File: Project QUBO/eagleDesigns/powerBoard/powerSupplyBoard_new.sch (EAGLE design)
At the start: 146 parts

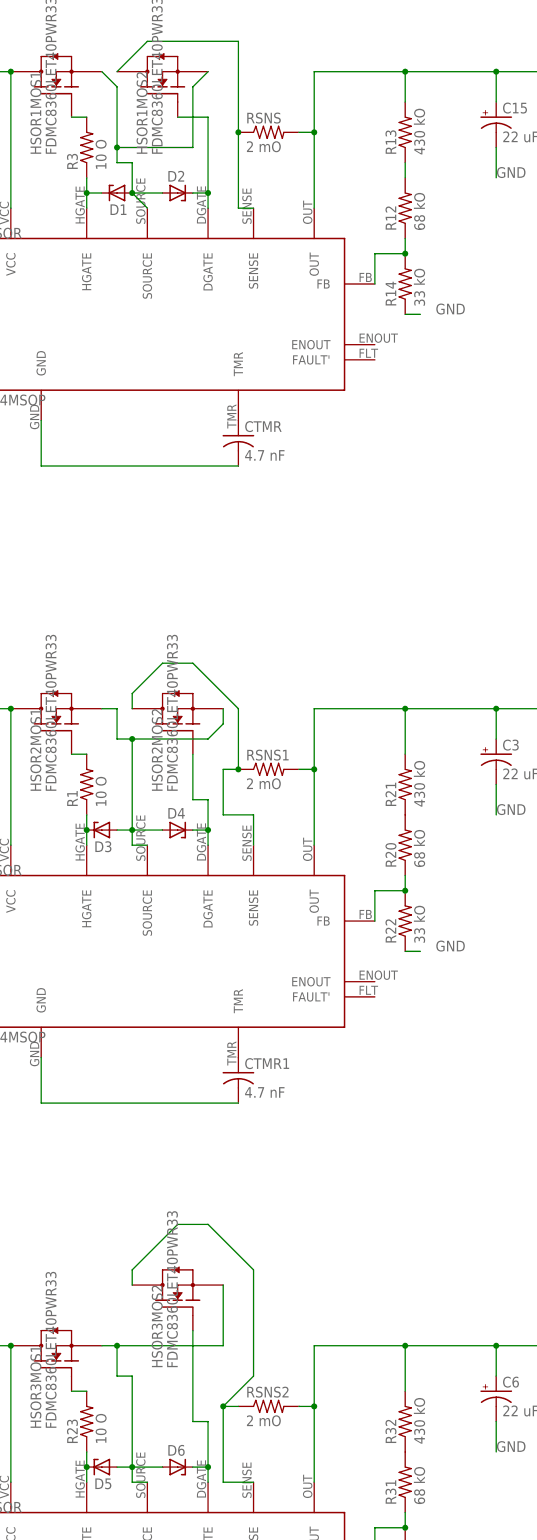
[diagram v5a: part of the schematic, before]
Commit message: got rid of sense resistor on psb
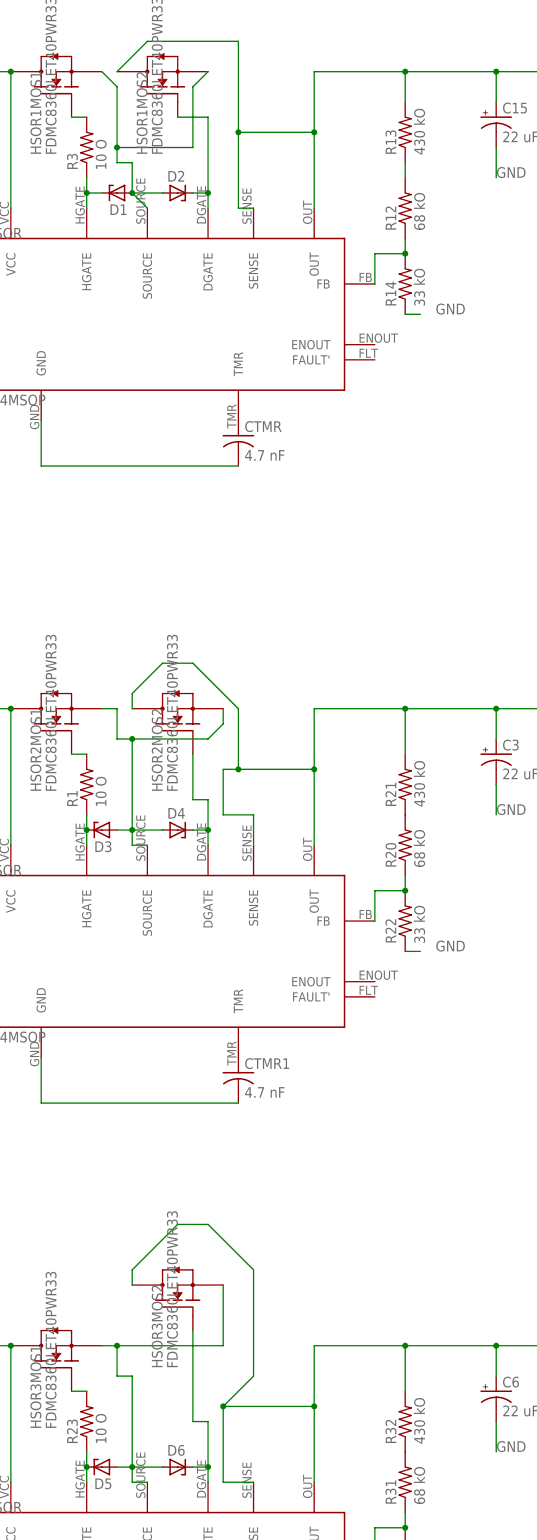
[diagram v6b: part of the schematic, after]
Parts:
- removed RSNS, RSNS1, RSNS2: 2 mO, resistor:R-US_R0805
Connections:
- removed net N$1: BAT1HSOR.SENSE, HSOR1MOS2.DRAIN, RSNS.1
- removed net N$43: BAT3HSOR.SENSE, HSOR3MOS2.DRAIN, RSNS2.1
- removed net N$5: BAT2HSOR.SENSE, HSOR2MOS2.DRAIN, RSNS1.1
- net BAT1HSOROUT: now also BAT1HSOR.SENSE, HSOR1MOS2.DRAIN; no longer RSNS.2
- net BAT2HSOROUT: now also BAT2HSOR.SENSE, HSOR2MOS2.DRAIN; no longer RSNS1.2
- net BAT3HSOROUT: now also BAT3HSOR.SENSE, HSOR3MOS2.DRAIN; no longer RSNS2.2
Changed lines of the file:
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@@
 <part name="R13" library="resistor" deviceset="R-US_" device="R0805" value="430 kO"/>
 <part name="R14" library="resistor" deviceset="R-US_" device="R0805" value="33 kO"/>
-<part name="RSNS" library="resistor" deviceset="R-US_" device="R0805" value="2 mO"/>
 <part name="CTMR" library="resistor" deviceset="C-US" device="C0805" value="4.7 nF"/>
 <part name="C15" library="resistor" deviceset="CPOL-US" device="F" value="22 uF"/>
@@
 <part name="R21" library="resistor" deviceset="R-US_" device="R0805" value="430 kO"/>
 <part name="R22" library="resistor" deviceset="R-US_" device="R0805" value="33 kO"/>
-<part name="RSNS1" library="resistor" deviceset="R-US_" device="R0805" value="2 mO"/>
 <part name="CTMR1" library="resistor" deviceset="C-US" device="C0805" value="4.7 nF"/>
 <part name="C3" library="resistor" deviceset="CPOL-US" device="F" value="22 uF"/>
@@
 <part name="R32" library="resistor" deviceset="R-US_" device="R0805" value="430 kO"/>
 <part name="R33" library="resistor" deviceset="R-US_" device="R0805" value="33 kO"/>
-<part name="RSNS2" library="resistor" deviceset="R-US_" device="R0805" value="2 mO"/>
 <part name="CTMR2" library="resistor" deviceset="C-US" device="C0805" value="4.7 nF"/>
 <part name="C6" library="resistor" deviceset="CPOL-US" device="F" value="22 uF"/>
@@
 <instance part="R13" gate="G$1" x="-116.84" y="121.92" rot="R90"/>
 <instance part="R14" gate="G$1" x="-116.84" y="96.52" rot="R90"/>
-<instance part="RSNS" gate="G$1" x="-139.7" y="121.92"/>
 <instance part="CTMR" gate="G$1" x="-144.78" y="71.12"/>
 <instance part="C15" gate="G$1" x="-101.6" y="124.46"/>
@@
 <instance part="R21" gate="G$1" x="-116.84" y="12.7" rot="R90"/>
 <instance part="R22" gate="G$1" x="-116.84" y="-10.16" rot="R90"/>
-<instance part="RSNS1" gate="G$1" x="-139.7" y="15.24"/>
 <instance part="CTMR1" gate="G$1" x="-144.78" y="-35.56"/>
 <instance part="C3" gate="G$1" x="-101.6" y="17.78"/>
@@
 <instance part="R32" gate="G$1" x="-116.84" y="-93.98" rot="R90"/>
 <instance part="R33" gate="G$1" x="-116.84" y="-116.84" rot="R90"/>
-<instance part="RSNS2" gate="G$1" x="-139.7" y="-91.44"/>
 <instance part="CTMR2" gate="G$1" x="-144.78" y="-142.24"/>
 <instance part="C6" gate="G$1" x="-101.6" y="-88.9"/>
@@
 <net name="BAT1HSOROUT" class="0">
 <segment>
-<pinref part="RSNS" gate="G$1" pin="2"/>
 <pinref part="BAT1HSOR" gate="G$1" pin="OUT"/>
-<wire x1="-134.62" y1="121.92" x2="-132.08" y2="121.92" width="0.1524" layer="91"/>
 <wire x1="-132.08" y1="121.92" x2="-132.08" y2="109.22" width="0.1524" layer="91"/>
 <wire x1="-132.08" y1="121.92" x2="-132.08" y2="132.08" width="0.1524" layer="91"/>
@@
 <junction x="-101.6" y="132.08"/>
 <pinref part="BAT1CS" gate="G$1" pin="IP+"/>
+<pinref part="BAT1HSOR" gate="G$1" pin="SENSE"/>
+<wire x1="-142.24" y1="109.22" x2="-144.78" y2="109.22" width="0.1524" layer="91"/>
+<wire x1="-144.78" y1="137.16" x2="-144.78" y2="121.92" width="0.1524" layer="91"/>
+<pinref part="HSOR1MOS2" gate="G$1" pin="DRAIN"/>
+<wire x1="-144.78" y1="121.92" x2="-144.78" y2="109.22" width="0.1524" layer="91"/>
+<wire x1="-165.1" y1="132.08" x2="-160.02" y2="137.16" width="0.1524" layer="91"/>
+<wire x1="-160.02" y1="137.16" x2="-144.78" y2="137.16" width="0.1524" layer="91"/>
+<wire x1="-132.08" y1="121.92" x2="-144.78" y2="121.92" width="0.1524" layer="91"/>
+<junction x="-144.78" y="121.92"/>
 </segment>
 </net>
@@
 </segment>
 </net>
-<net name="N$5" class="0">
-<segment>
-<pinref part="BAT2HSOR" gate="G$1" pin="SENSE"/>
-<wire x1="-142.24" y1="7.62" x2="-142.24" y2="2.54" width="0.1524" layer="91"/>
-<wire x1="-142.24" y1="7.62" x2="-147.32" y2="7.62" width="0.1524" layer="91"/>
-<wire x1="-147.32" y1="7.62" x2="-147.32" y2="15.24" width="0.1524" layer="91"/>
-<pinref part="RSNS1" gate="G$1" pin="1"/>
-<wire x1="-144.78" y1="15.24" x2="-147.32" y2="15.24" width="0.1524" layer="91"/>
-<pinref part="HSOR2MOS2" gate="G$1" pin="DRAIN"/>
-<wire x1="-162.56" y1="25.4" x2="-162.56" y2="27.94" width="0.1524" layer="91"/>
-<wire x1="-162.56" y1="27.94" x2="-157.48" y2="33.02" width="0.1524" layer="91"/>
-<wire x1="-157.48" y1="33.02" x2="-152.4" y2="33.02" width="0.1524" layer="91"/>
-<wire x1="-152.4" y1="33.02" x2="-144.78" y2="25.4" width="0.1524" layer="91"/>
-<wire x1="-144.78" y1="25.4" x2="-144.78" y2="15.24" width="0.1524" layer="91"/>
-<junction x="-144.78" y="15.24"/>
-</segment>
-</net>
 <net name="N$6" class="0">
 <segment>
@@
 <net name="BAT2HSOROUT" class="0">
 <segment>
-<pinref part="RSNS1" gate="G$1" pin="2"/>
 <pinref part="BAT2HSOR" gate="G$1" pin="OUT"/>
-<wire x1="-134.62" y1="15.24" x2="-132.08" y2="15.24" width="0.1524" layer="91"/>
 <wire x1="-132.08" y1="15.24" x2="-132.08" y2="2.54" width="0.1524" layer="91"/>
 <wire x1="-132.08" y1="15.24" x2="-132.08" y2="25.4" width="0.1524" layer="91"/>
@@
 <junction x="-101.6" y="25.4"/>
 <pinref part="BAT2CS" gate="G$1" pin="IP+"/>
+<pinref part="BAT2HSOR" gate="G$1" pin="SENSE"/>
+<wire x1="-142.24" y1="7.62" x2="-142.24" y2="2.54" width="0.1524" layer="91"/>
+<wire x1="-142.24" y1="7.62" x2="-147.32" y2="7.62" width="0.1524" layer="91"/>
+<wire x1="-147.32" y1="7.62" x2="-147.32" y2="15.24" width="0.1524" layer="91"/>
+<wire x1="-144.78" y1="15.24" x2="-147.32" y2="15.24" width="0.1524" layer="91"/>
+<pinref part="HSOR2MOS2" gate="G$1" pin="DRAIN"/>
+<wire x1="-162.56" y1="25.4" x2="-162.56" y2="27.94" width="0.1524" layer="91"/>
+<wire x1="-162.56" y1="27.94" x2="-157.48" y2="33.02" width="0.1524" layer="91"/>
+<wire x1="-157.48" y1="33.02" x2="-152.4" y2="33.02" width="0.1524" layer="91"/>
+<wire x1="-152.4" y1="33.02" x2="-144.78" y2="25.4" width="0.1524" layer="91"/>
+<wire x1="-144.78" y1="25.4" x2="-144.78" y2="15.24" width="0.1524" layer="91"/>
+<wire x1="-132.08" y1="15.24" x2="-144.78" y2="15.24" width="0.1524" layer="91"/>
+<junction x="-144.78" y="15.24"/>
 </segment>
 </net>
@@
 <net name="BAT3HSOROUT" class="0">
 <segment>
-<pinref part="RSNS2" gate="G$1" pin="2"/>
 <pinref part="BAT3HSOR" gate="G$1" pin="OUT"/>
-<wire x1="-134.62" y1="-91.44" x2="-132.08" y2="-91.44" width="0.1524" layer="91"/>
 <wire x1="-132.08" y1="-91.44" x2="-132.08" y2="-104.14" width="0.1524" layer="91"/>
 <wire x1="-132.08" y1="-91.44" x2="-132.08" y2="-81.28" width="0.1524" layer="91"/>
@@
 <junction x="-101.6" y="-81.28"/>
 <pinref part="BAT3CS" gate="G$1" pin="IP+"/>
+<pinref part="BAT3HSOR" gate="G$1" pin="SENSE"/>
+<wire x1="-142.24" y1="-104.14" x2="-147.32" y2="-104.14" width="0.1524" layer="91"/>
+<wire x1="-147.32" y1="-104.14" x2="-147.32" y2="-91.44" width="0.1524" layer="91"/>
+<pinref part="HSOR3MOS2" gate="G$1" pin="DRAIN"/>
+<wire x1="-162.56" y1="-71.12" x2="-162.56" y2="-68.58" width="0.1524" layer="91"/>
+<wire x1="-162.56" y1="-68.58" x2="-154.94" y2="-60.96" width="0.1524" layer="91"/>
+<wire x1="-154.94" y1="-60.96" x2="-149.86" y2="-60.96" width="0.1524" layer="91"/>
+<wire x1="-149.86" y1="-60.96" x2="-142.24" y2="-68.58" width="0.1524" layer="91"/>
+<wire x1="-142.24" y1="-68.58" x2="-142.24" y2="-86.36" width="0.1524" layer="91"/>
+<wire x1="-142.24" y1="-86.36" x2="-147.32" y2="-91.44" width="0.1524" layer="91"/>
+<junction x="-147.32" y="-91.44"/>
+<wire x1="-147.32" y1="-91.44" x2="-132.08" y2="-91.44" width="0.1524" layer="91"/>
 </segment>
 </net>
@@
 </segment>
 </net>
-<net name="N$1" class="0">
-<segment>
-<pinref part="RSNS" gate="G$1" pin="1"/>
-<wire x1="-144.78" y1="121.92" x2="-144.78" y2="109.22" width="0.1524" layer="91"/>
-<pinref part="BAT1HSOR" gate="G$1" pin="SENSE"/>
-<wire x1="-142.24" y1="109.22" x2="-144.78" y2="109.22" width="0.1524" layer="91"/>
-<wire x1="-144.78" y1="137.16" x2="-144.78" y2="121.92" width="0.1524" layer="91"/>
-<junction x="-144.78" y="121.92"/>
-<pinref part="HSOR1MOS2" gate="G$1" pin="DRAIN"/>
-<wire x1="-165.1" y1="132.08" x2="-160.02" y2="137.16" width="0.1524" layer="91"/>
-<wire x1="-160.02" y1="137.16" x2="-144.78" y2="137.16" width="0.1524" layer="91"/>
-</segment>
-</net>
 <net name="N$11" class="0">
 <segment>
@@
 </segment>
 </net>
-<net name="N$43" class="0">
-<segment>
-<pinref part="RSNS2" gate="G$1" pin="1"/>
-<wire x1="-144.78" y1="-91.44" x2="-147.32" y2="-91.44" width="0.1524" layer="91"/>
-<pinref part="BAT3HSOR" gate="G$1" pin="SENSE"/>
-<wire x1="-142.24" y1="-104.14" x2="-147.32" y2="-104.14" width="0.1524" layer="91"/>
-<wire x1="-147.32" y1="-104.14" x2="-147.32" y2="-91.44" width="0.1524" layer="91"/>
-<pinref part="HSOR3MOS2" gate="G$1" pin="DRAIN"/>
-<wire x1="-162.56" y1="-71.12" x2="-162.56" y2="-68.58" width="0.1524" layer="91"/>
-<wire x1="-162.56" y1="-68.58" x2="-154.94" y2="-60.96" width="0.1524" layer="91"/>
-<wire x1="-154.94" y1="-60.96" x2="-149.86" y2="-60.96" width="0.1524" layer="91"/>
-<wire x1="-149.86" y1="-60.96" x2="-142.24" y2="-68.58" width="0.1524" layer="91"/>
-<wire x1="-142.24" y1="-68.58" x2="-142.24" y2="-86.36" width="0.1524" layer="91"/>
-<wire x1="-142.24" y1="-86.36" x2="-147.32" y2="-91.44" width="0.1524" layer="91"/>
-<junction x="-147.32" y="-91.44"/>
-</segment>
-</net>

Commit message: 
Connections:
- removed net GND: 12VCS.GND, 12VREG.GND1, 12VREG.GND2, 16VCS.GND, 16V_CON.P$1, 3.3VCS.GND, 3.3VREG.GND1, 3.3VREG.GND2, 5VCS.GND, 5VREG.AGND, 5VREG.PGND, 5VREG.SYNC, ADC.COM, ADC.F0, ADC.GND, ADC.REF-, BAT1CS.GND, BAT1HSOR.GND, BAT2CS.GND, BAT2HSOR.GND, BAT3CS.GND, BAT3HSOR.GND, C1.2, C12.2, C15.-, C2.2, C3.-, C4.2, C5.2, C6.-, CTMR.2, CTMR1.2, CTMR2.2, C_0_12V.-, C_0_3.3V.-, C_1_12V.2, C_1_3.3V.2, C_BYP.2, C_BYP1.2, C_BYP2.2, C_BYP3.2, C_BYP4.2, C_BYP5.2, C_BYP6.2, C_BYP7.2, C_F.2, C_F1.2, C_F2.2, C_F3.2, C_F4.2, C_F5.2, C_F6.2, C_IN_5V.2, C_OUT_5V.-, DVL_12VREG.-VIN, HIGHSIDEMOS1.S, HIGHSIDEMOS2.S, HIGHSIDEMOS3.S, IOEXPANDER.GND, JP1.P$12, JP1.P$15, JP1.P$18, JP1.P$24, JP1.P$33, JP1.P$34, JP1.P$37, JP1.P$39, JP1.P$4, JP1.P$40, JP1.P$44, JP1.P$64, R14.1, R17.1, R19.1, R22.1, R28.1, R30.1, R33.1, R35.1, R37.1, R39.1, R41.1, R43.1, R45.1, R47.1, R9.1, REN_B.1, REN_B.2, REN_H.1, REN_T.2, RFBB.2, R_LOAD.1, R_SET12V.1, R_SET3.3V.1, TEMP_SENSOR_1.GND, TEMP_SENSOR_2.GND, U$10.GND, U$14.S, U$15.S, U$16.GND, U$17.PWR, U$18.GND, U$5.A, U$5.C, U$6.GND, U$9.GND
- removed net N$100: JP1.P$36
- removed net SCL1: ADC.SCL, IOEXPANDER.SCL, JP1.P$10
- removed net SDA1: ADC.SDA, IOEXPANDER.SDA, JP1.P$9
- new net AGND: 12VCS.GND, 12VREG.GND1, 12VREG.GND2, 16VCS.GND, 16V_CON.P$1, 3.3VCS.GND, 3.3VREG.GND1, 3.3VREG.GND2, 5VCS.GND, 5VREG.AGND, 5VREG.PGND, 5VREG.SYNC, ADC.F0, BAT1CS.GND, BAT1HSOR.GND, BAT2CS.GND, BAT2HSOR.GND, BAT3CS.GND, BAT3HSOR.GND, C1.2, C12.2, C15.-, C2.2, C3.-, C4.2, C5.2, C6.-, CTMR.2, CTMR1.2, CTMR2.2, C_0_12V.-, C_0_3.3V.-, C_1_12V.2, C_1_3.3V.2, C_BYP.2, C_BYP1.2, C_BYP2.2, C_BYP3.2, C_BYP4.2, C_BYP5.2, C_BYP6.2, C_BYP7.2, C_F.2, C_F1.2, C_F2.2, C_F3.2, C_F4.2, C_F5.2, C_F6.2, C_IN_5V.2, C_OUT_5V.-, DVL_12VREG.-VIN, HIGHSIDEMOS1.S, HIGHSIDEMOS2.S, HIGHSIDEMOS3.S, JP1.P$19, JP1.P$20, JP1.P$39, JP1.P$40, JP1.P$59, JP1.P$60, JP1.P$79, JP1.P$80, R14.1, R17.1, R19.1, R22.1, R28.1, R30.1, R33.1, R35.1, R37.1, R39.1, R41.1, R43.1, R45.1, R47.1, R9.1, REN_B.1, REN_B.2, REN_H.1, REN_T.2, RFBB.2, R_LOAD.1, R_SET12V.1, R_SET3.3V.1, TEMP_SENSOR_1.GND, TEMP_SENSOR_2.GND, U$10.GND, U$14.S, U$15.S, U$16.GND, U$17.PWR, U$18.GND, U$5.A, U$5.C, U$6.GND, U$9.GND
- new net DGND: ADC.COM, ADC.GND, ADC.REF-, IOEXPANDER.GND, JP1.P$1, JP1.P$15, JP1.P$21, JP1.P$25, JP1.P$32, JP1.P$35, JP1.P$47, JP1.P$55, JP1.P$63, JP1.P$75
- new net INT_SCL: ADC.SCL, IOEXPANDER.SCL, JP1.P$66
- new net INT_SDA: ADC.SDA, IOEXPANDER.SDA, JP1.P$65
- net 12V: now also JP1.P$16, JP1.P$36, JP1.P$56, JP1.P$76; no longer JP1.P$1, JP1.P$21, JP1.P$41, JP1.P$61
- net 3.3V: now also JP1.P$18, JP1.P$38, JP1.P$58, JP1.P$78; no longer JP1.P$23, JP1.P$3, JP1.P$43, JP1.P$63
- net 5V: now also JP1.P$17, JP1.P$37, JP1.P$57, JP1.P$77; no longer JP1.P$2, JP1.P$22, JP1.P$42, JP1.P$62

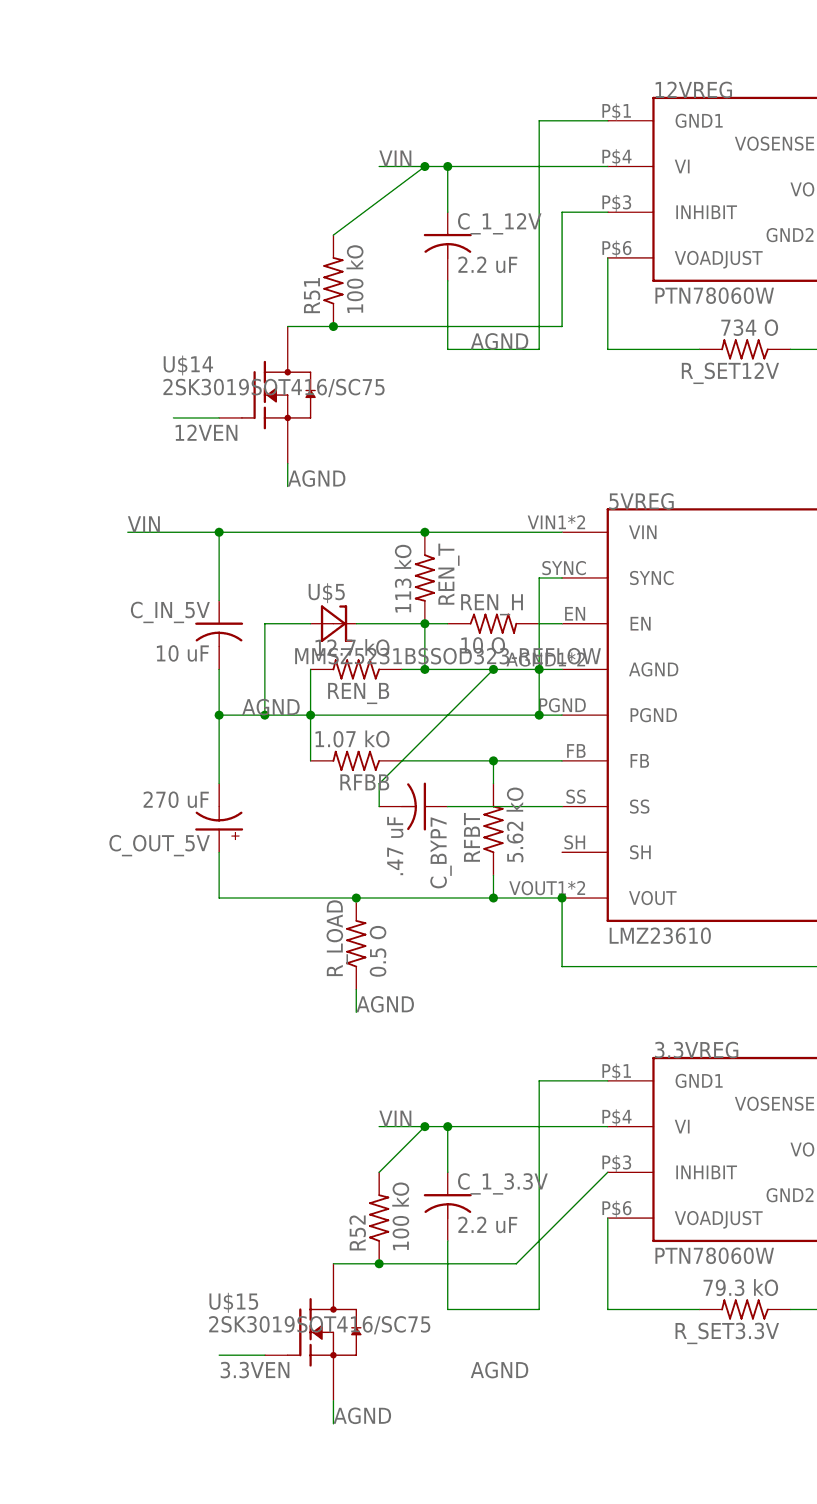
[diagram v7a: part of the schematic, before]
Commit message: 
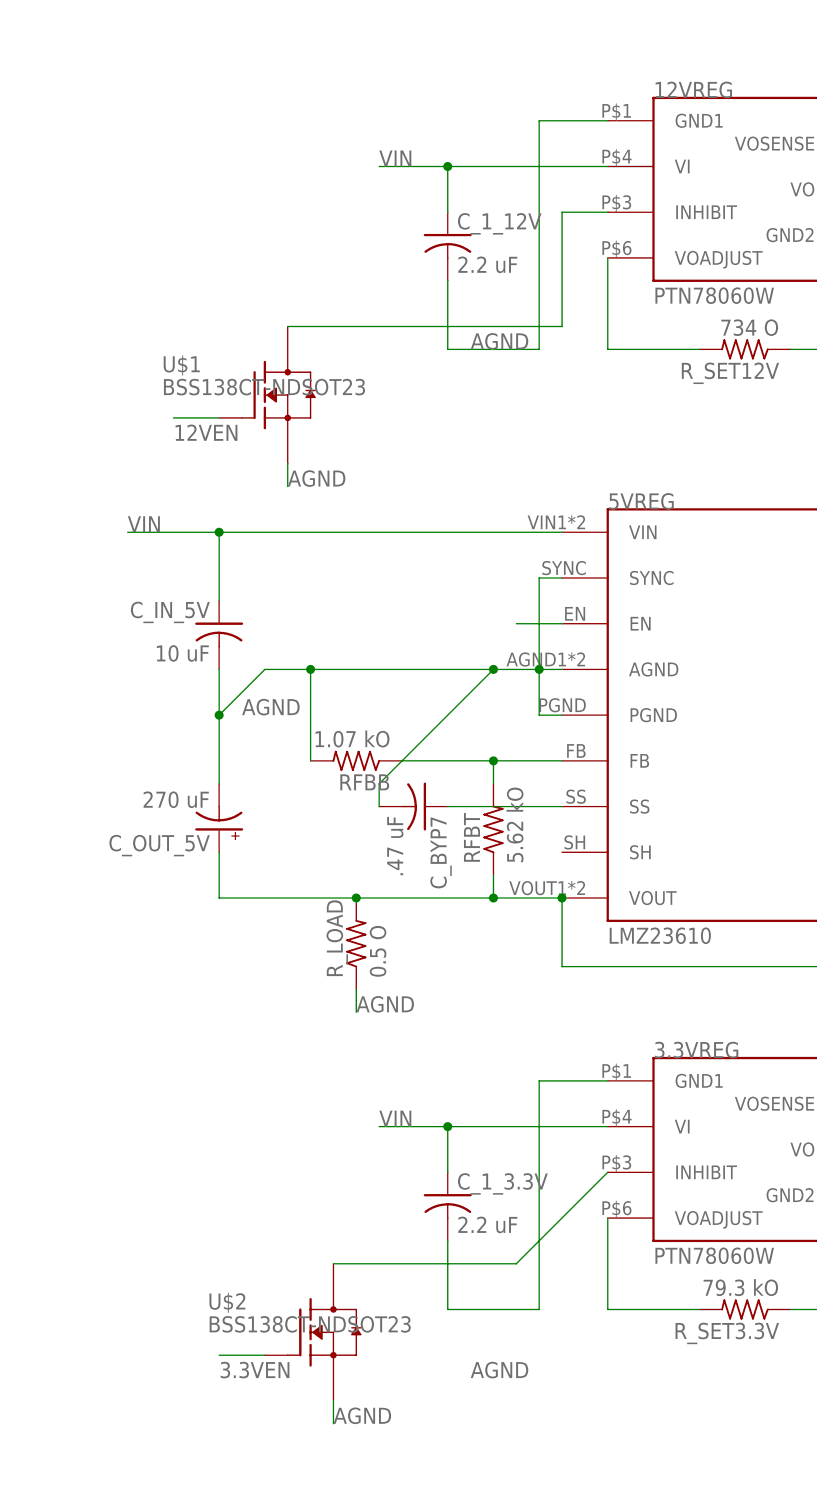
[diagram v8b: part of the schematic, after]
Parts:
- removed R51, R52: 100 kO, resistor:R-US_R0805
- removed REN_B: 12.7 kO, resistor:R-US_R0805
- removed REN_H: 10 O, resistor:R-US_R0805
- removed REN_T: 113 kO, resistor:R-US_R0805
- removed U$14, U$15: 2SK3019SOT416/SC75, transistor-fet:2SK3019SOT416/SC75
- removed U$5: MMSZ5231BSSOD323-REFLOW, diode:MMSZ5231BSSOD323-REFLOW
- added U$1, U$2: BSS138CT-NDSOT23, transistor-fet:BSS138CT-NDSOT23
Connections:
- removed net N$58: 5VREG.EN, REN_H.2
- new net N$41: 5VREG.EN
- net 12VEN: now also U$1.G; no longer U$14.G
- net 3.3VEN: now also U$2.G; no longer U$15.G
- net AGND: now also U$1.S, U$2.S; no longer REN_B.1, REN_B.2, REN_H.1, REN_T.2, U$14.S, U$15.S, U$5.A, U$5.C
- net N$87: now also U$1.D; no longer R51.1, U$14.D
- net N$89: now also U$2.D; no longer R52.1, U$15.D
- net VIN: no longer R51.2, R52.2, REN_T.1
